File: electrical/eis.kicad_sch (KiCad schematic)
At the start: 52 parts

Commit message: Swapped red/yellow on CHT/EGT to match rewiring of connector.
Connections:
- net Red: now also CHT.1 (Pin_1), CHT.1 (Pin_1), CHT.13 (Pin_13), CHT1.2, COWL_TEMP.2, EGT.1 (Pin_1), EGT.1 (Pin_1), EGT.13 (Pin_13), EGT1.2, GEA24.P242_24 (CHT1_HI), GEA24.P242_25 (EGT1_HI), OIL_AIR_PRE_TEMP.2; no longer CHT.14 (Pin_14), CHT.2 (Pin_2), CHT.2 (Pin_2), CHT1.1, COWL_TEMP.1, EGT.14 (Pin_14), EGT.2 (Pin_2), EGT.2 (Pin_2), EGT1.1, GEA24.P242_12 (CHT1_LO), GEA24.P242_13 (EGT1_LO), OIL_AIR_PRE_TEMP.1
- net Yellow: now also CHT.14 (Pin_14), CHT.2 (Pin_2), CHT.2 (Pin_2), CHT1.1, COWL_TEMP.1, EGT.14 (Pin_14), EGT.2 (Pin_2), EGT.2 (Pin_2), EGT1.1, GEA24.P242_12 (CHT1_LO), GEA24.P242_13 (EGT1_LO), OIL_AIR_PRE_TEMP.1; no longer CHT.1 (Pin_1), CHT.1 (Pin_1), CHT.13 (Pin_13), CHT1.2, COWL_TEMP.2, EGT.1 (Pin_1), EGT.1 (Pin_1), EGT.13 (Pin_13), EGT1.2, GEA24.P242_24 (CHT1_HI), GEA24.P242_25 (EGT1_HI), OIL_AIR_PRE_TEMP.2
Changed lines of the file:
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@@
 	(title_block
 		(title "EIS")
-		(date "2025-11-19")
-		(rev "1.2.8")
+		(date "2025-12-19")
+		(rev "1.2.10")
 		(company "N78HR")
 	)
@@
 		)
 	)
-	(label "Yellow"
+	(label "Red"
 		(at 199.39 106.68 0)
 		(effects
@@
 		)
 	)
-	(label "Red"
+	(label "Yellow"
 		(at 67.31 81.28 0)
 		(effects
@@
 		)
 	)
-	(label "Yellow"
+	(label "Red"
 		(at 67.31 78.74 0)
 		(effects
@@
 		)
 	)
-	(label "Yellow"
+	(label "Red"
 		(at 198.12 77.47 0)
 		(effects
@@
 		)
 	)
-	(label "Red"
+	(label "Yellow"
 		(at 199.39 109.22 0)
 		(effects
@@
 		)
 	)
-	(label "Yellow"
+	(label "Red"
 		(at 199.39 137.16 0)
 		(effects
@@
 		)
 	)
-	(label "Red"
+	(label "Yellow"
 		(at 199.39 139.7 0)
 		(effects
@@
 		)
 	)
-	(label "Red"
+	(label "Yellow"
 		(at 198.12 49.53 0)
 		(effects
@@
 		)
 	)
-	(label "Red"
+	(label "Yellow"
 		(at 198.12 80.01 0)
 		(effects
@@
 		)
 	)
+	(label "Red"
+		(at 67.31 46.99 0)
+		(effects
+			(font
+				(size 1.27 1.27)
+			)
+			(justify left bottom)
+		)
+	)
 	(label "Yellow"
-		(at 67.31 46.99 0)
+		(at 67.31 49.53 0)
 		(effects
 			(font
@@
 	)
 	(label "Red"
-		(at 67.31 49.53 0)
-		(effects
-			(font
-				(size 1.27 1.27)
-			)
-			(justify left bottom)
-		)
-	)
-	(label "Yellow"
 		(at 198.12 46.99 0)
 		(effects

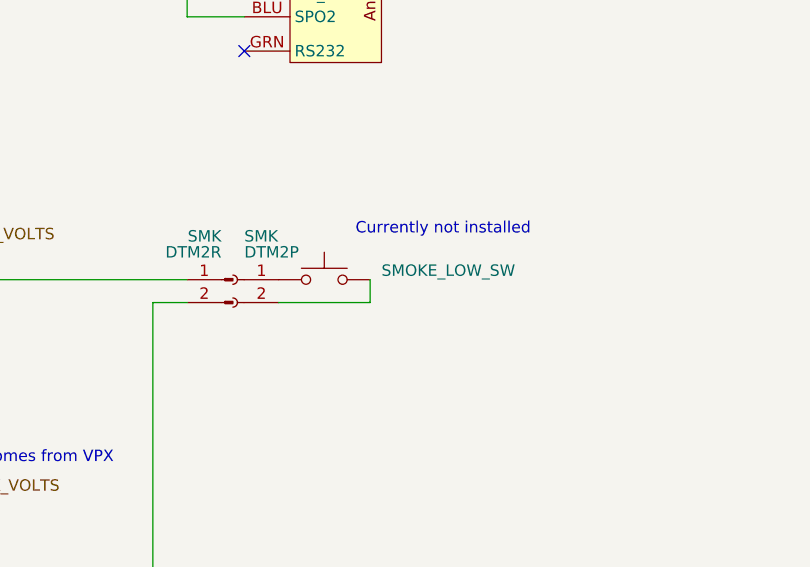
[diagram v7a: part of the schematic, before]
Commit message: adds battery fault
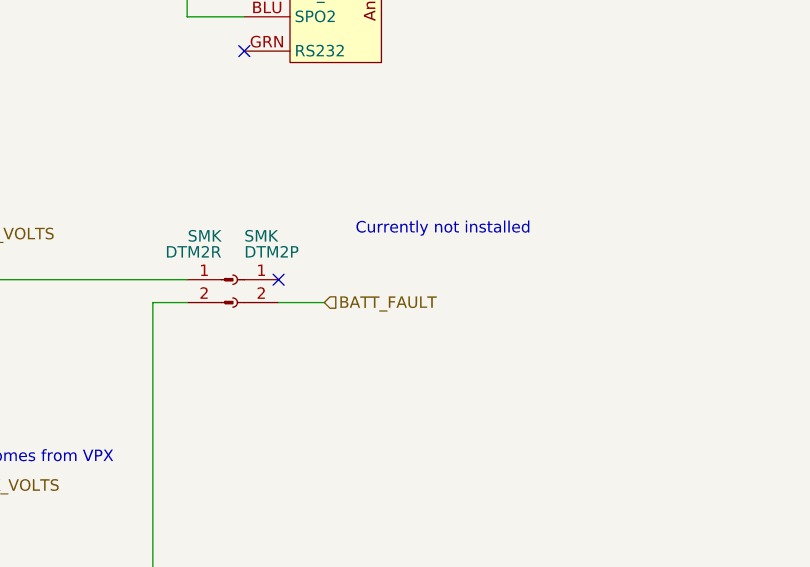
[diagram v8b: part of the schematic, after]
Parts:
- removed SMOKE_LOW_SW: FLOAT_SENSOR, symbol Switch:SW_Push
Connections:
- net BATT_FAULT: now reaches SMK.2 (Pin_2)
- no-connect marks 27 -> 28
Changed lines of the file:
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@@
 	(title_block
 		(title "EIS")
-		(date "2025-12-19")
-		(rev "1.2.10")
+		(date "2026-04-02")
+		(rev "1.2.13")
 		(company "N78HR")
 	)
@@
 	)
 	(no_connect
+		(at 115.57 289.56)
+	)
+	(no_connect
 		(at 67.31 134.62)
 	)
@@
 	(wire
 		(pts
+			(xy 115.57 292.1) (xy 120.65 292.1)
+		)
+		(stroke
+			(width 0)
+			(type default)
+		)
+	)
+	(wire
+		(pts
 			(xy 147.32 129.54) (xy 189.23 129.54)
 		)
@@
 	(wire
 		(pts
-			(xy 115.57 292.1) (xy 125.73 292.1)
-		)
-		(stroke
-			(width 0)
-			(type default)
-		)
-	)
-	(wire
-		(pts
 			(xy 210.82 67.31) (xy 210.82 69.85)
 		)
@@
 	(wire
 		(pts
-			(xy 125.73 289.56) (xy 125.73 292.1)
-		)
-		(stroke
-			(width 0)
-			(type default)
-		)
-	)
-	(wire
-		(pts
 			(xy 67.31 96.52) (xy 151.13 96.52)
 		)
@@
 		)
 	)
+	(hierarchical_label "BATT_FAULT"
+		(shape input)
+		(at 120.65 292.1 0)
+		(effects
+			(font
+				(size 1.27 1.27)
+			)
+			(justify left)
+		)
+	)
 	(hierarchical_label "GEA24_PWR"
 		(shape input)
@@
 					(unit 1)
 				)
-			)
-		)
-	)
-	(symbol
-		(lib_id "Switch:SW_Push")
-		(at 120.65 289.56 0)
-		(unit 1)
-		(exclude_from_sim no)
-		(in_bom yes)
-		(on_board yes)
-		(dnp no)
-		(property "Reference" "SMOKE_LOW_SW"
-			(at 127 288.544 0)
-			(effects
-				(font
-					(size 1.27 1.27)
-				)
-				(justify left)
-			)
-		)
-		(property "Value" "FLOAT_SENSOR"
-			(at 120.65 284.48 0)
-			(effects
-				(font
-					(size 1.27 1.27)
-				)
-				(hide yes)
-			)
-		)
-		(property "Footprint" ""
-			(at 120.65 284.48 0)
-			(effects
-				(font
-					(size 1.27 1.27)
-				)
-				(hide yes)
-			)
-		)
-		(property "Datasheet" "~"
-			(at 120.65 284.48 0)
-			(effects
-				(font
-					(size 1.27 1.27)
-				)
-				(hide yes)
-			)
-		)
-		(property "Description" ""
-			(at 120.65 289.56 0)
-			(effects
-				(font
-					(size 1.27 1.27)
-				)
-			)
-		)
-		(pin "1"
-		)
-		(pin "2"
-		)
-		(instances
-			(project "electrical"
-				(path "/e8ec215a-dbe2-4eba-a577-e50a0a128049/72184f52-5cc1-469a-bd6f-4bd63aea59bf"
-					(reference "SMOKE_LOW_SW")
-					(unit 1)
-				)
